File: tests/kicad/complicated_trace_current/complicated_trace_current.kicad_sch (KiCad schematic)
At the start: 2 parts

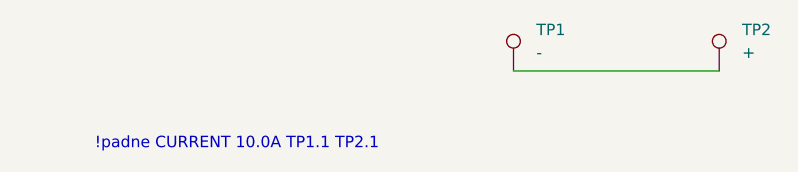
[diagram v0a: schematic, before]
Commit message: feat: Richer directive syntax
This commit adds support for named directive parameters. No more
guessing which parameter is the positive terminal positive and which is the
negative terminal!
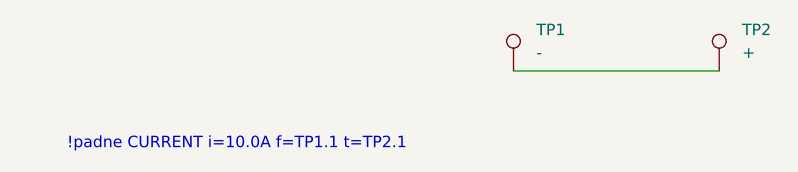
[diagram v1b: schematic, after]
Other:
- note added: "!padne CURRENT i=10.0A f=TP1.1 t=TP2.1"
- note removed: "!padne CURRENT 10.0A TP1.1 TP2.1"
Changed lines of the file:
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@@
 		)
 	)
-	(text "!padne CURRENT 10.0A TP1.1 TP2.1"
+	(text "!padne CURRENT i=10.0A f=TP1.1 t=TP2.1"
 		(exclude_from_sim no)
 		(at 79.756 107.188 0)
